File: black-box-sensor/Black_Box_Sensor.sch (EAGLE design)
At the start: 42 parts, among them J1 104031-0811, J2 UX60-MB-5S8, J3 B4B-PH-SM4-TBT(LF)(SN), U1 ADXL375, U2 ADXL375, U3 ATMEGA32U4-AU, U4 FXAS21002CQR1, U5 MIC5504-3.3YM5-TR, U6 NL27WZ32USG, U8 AD8426ACPZ-WP

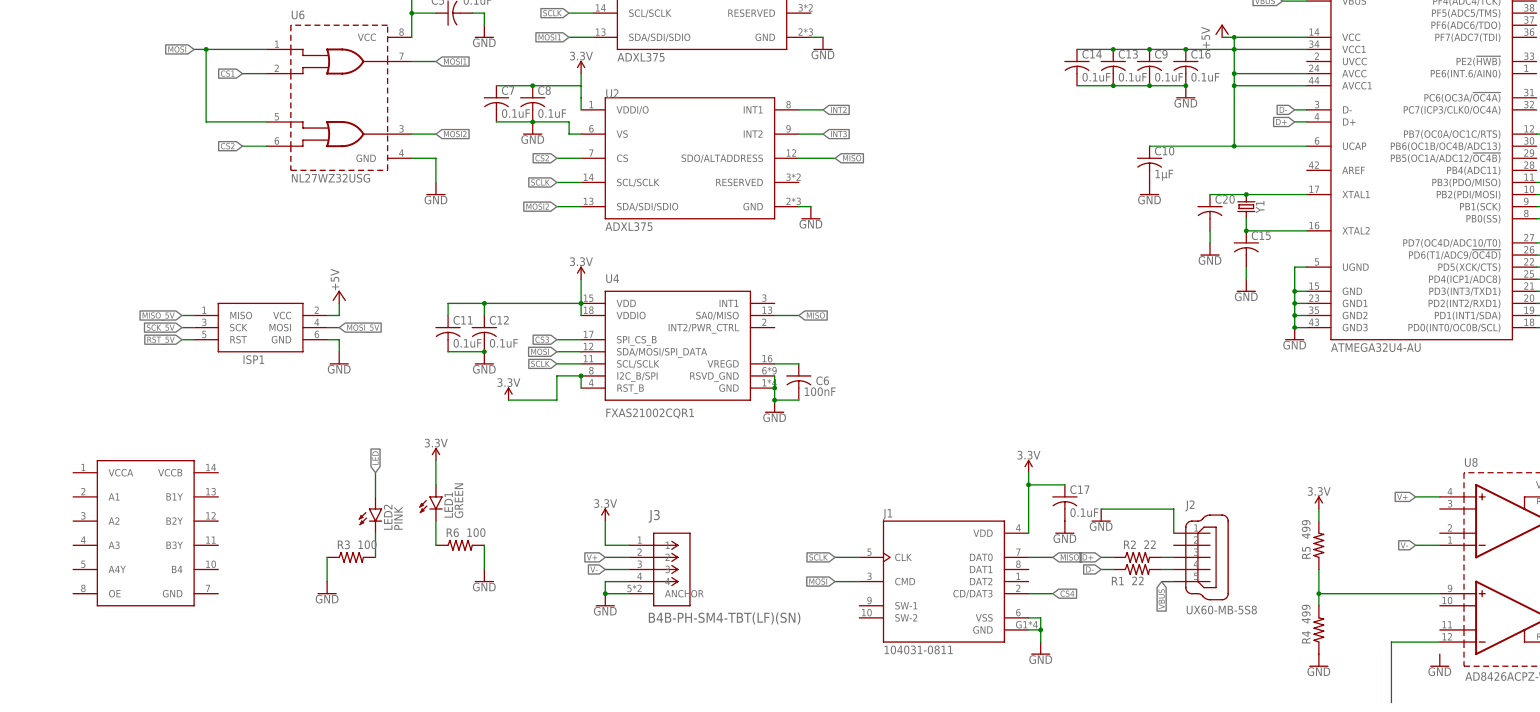
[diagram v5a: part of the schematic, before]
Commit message: label pins on level shifter
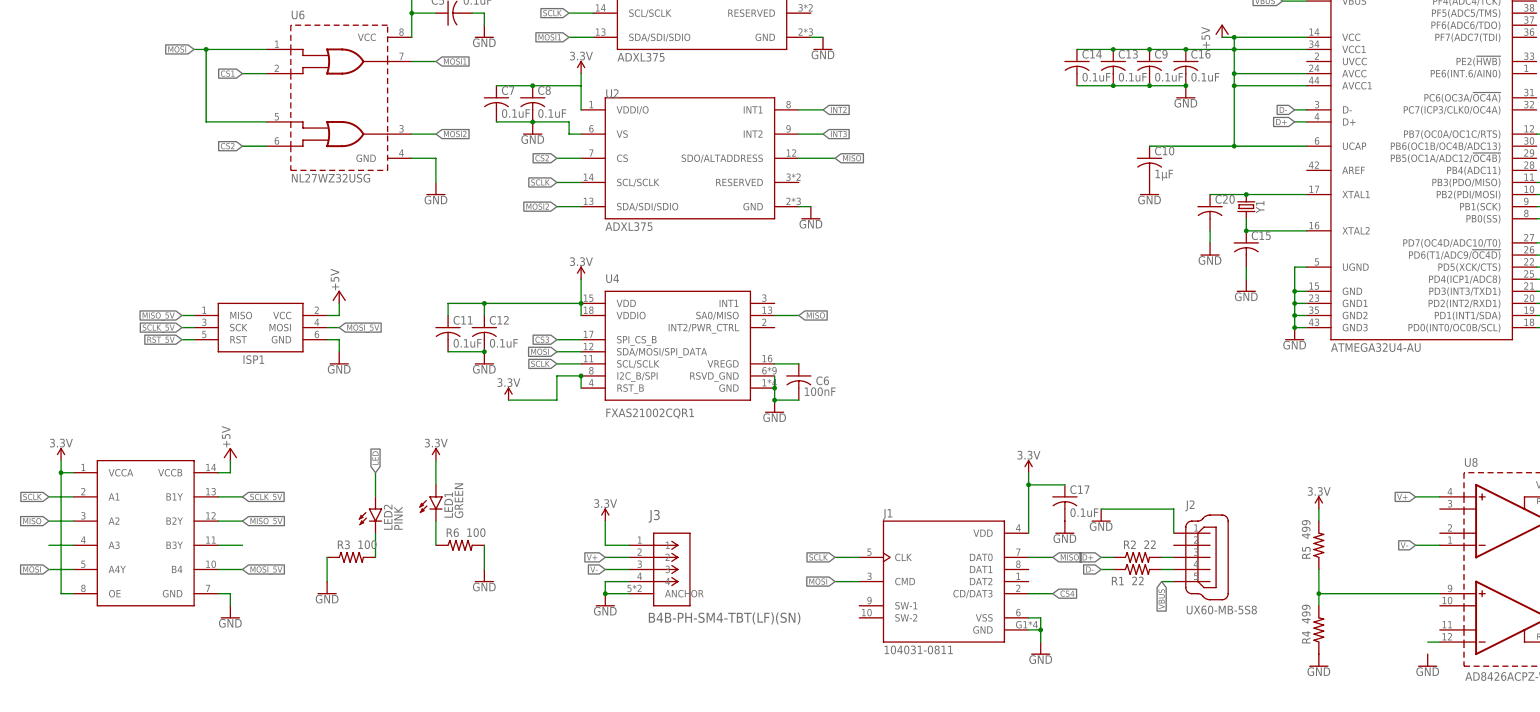
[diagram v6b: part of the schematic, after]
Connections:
- removed net SCK_5V: ISP1.SCK
- new net N$10: U$1.B3Y
- new net N$13: U$1.A3
- net +5V: now also U$1.VCCB
- net 3.3V: now also U$1.OE, U$1.VCCA
- net GND: now also U$1.GND
- net MISO: now also U$1.A2
- net MISO_5V: now also U$1.B2Y
- net MOSI: now also U$1.A4Y
- net MOSI_5V: now also U$1.B4
- net SCLK: now also U$1.A1
- net SCLK_5V: now also ISP1.SCK, U$1.B1Y
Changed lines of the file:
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@@
 <part name="GND27" library="SparkFun-PowerSymbols" deviceset="GND" device=""/>
 <part name="U$1" library="BBS_Library" deviceset="TXU0304" device=""/>
+<part name="GND28" library="SparkFun-PowerSymbols" deviceset="GND" device=""/>
+<part name="SUPPLY9" library="SparkFun-PowerSymbols" deviceset="3.3V" device=""/>
+<part name="P+4" library="supply1" library_urn="urn:adsk.eagle:library:371" deviceset="+5V" device=""/>
 </parts>
 <sheets>
@@
 <attribute name="NAME" x="-48.26" y="2.54" size="1.778" layer="95"/>
 </instance>
-<instance part="GND26" gate="1" x="203.2" y="-60.96" smashed="yes">
-<attribute name="VALUE" x="203.2" y="-61.214" size="1.778" layer="96" align="top-center"/>
+<instance part="GND26" gate="1" x="200.66" y="-60.96" smashed="yes">
+<attribute name="VALUE" x="200.66" y="-61.214" size="1.778" layer="96" align="top-center"/>
 </instance>
 <instance part="Y1" gate="G$1" x="162.56" y="35.56" smashed="yes" rot="R270">
@@
 </instance>
 <instance part="U$1" gate="G$1" x="-68.58" y="-33.02" smashed="yes"/>
+<instance part="GND28" gate="1" x="-50.8" y="-50.8" smashed="yes">
+<attribute name="VALUE" x="-50.8" y="-51.054" size="1.778" layer="96" align="top-center"/>
+</instance>
+<instance part="SUPPLY9" gate="G$1" x="-86.36" y="-17.78" smashed="yes">
+<attribute name="VALUE" x="-86.36" y="-14.986" size="1.778" layer="96" align="bottom-center"/>
+</instance>
+<instance part="P+4" gate="1" x="-50.8" y="-15.24" smashed="yes">
+<attribute name="VALUE" x="-50.8" y="-15.24" size="1.778" layer="96" rot="R90"/>
+</instance>
 </instances>
 <busses>
@@
 <pinref part="GND27" gate="1" pin="GND"/>
 </segment>
+<segment>
+<pinref part="U$1" gate="G$1" pin="GND"/>
+<wire x1="-53.34" y1="-45.72" x2="-50.8" y2="-45.72" width="0.1524" layer="91"/>
+<wire x1="-50.8" y1="-45.72" x2="-50.8" y2="-48.26" width="0.1524" layer="91"/>
+<pinref part="GND28" gate="1" pin="GND"/>
+</segment>
 </net>
 <net name="3.3V" class="0">
@@
 <segment>
 <pinref part="U2" gate="ADXL375BCCZ-RL7" pin="VDDI/O"/>
-<wire x1="22.86" y1="55.88" x2="22.86" y2="58.42" width="0.1524" layer="91"/>
 <pinref part="C8" gate="G$1" pin="1"/>
-<wire x1="22.86" y1="58.42" x2="22.86" y2="60.96" width="0.1524" layer="91"/>
+<wire x1="22.86" y1="55.88" x2="22.86" y2="60.96" width="0.1524" layer="91"/>
 <wire x1="22.86" y1="60.96" x2="12.7" y2="60.96" width="0.1524" layer="91"/>
 <pinref part="C7" gate="G$1" pin="1"/>
@@
 <pinref part="SUPPLY3" gate="G$1" pin="3.3V"/>
 </segment>
+<segment>
+<pinref part="U$1" gate="G$1" pin="VCCA"/>
+<wire x1="-83.82" y1="-20.32" x2="-86.36" y2="-20.32" width="0.1524" layer="91"/>
+<wire x1="-86.36" y1="-20.32" x2="-86.36" y2="-17.78" width="0.1524" layer="91"/>
+<pinref part="U$1" gate="G$1" pin="OE"/>
+<wire x1="-83.82" y1="-45.72" x2="-86.36" y2="-45.72" width="0.1524" layer="91"/>
+<wire x1="-86.36" y1="-45.72" x2="-86.36" y2="-20.32" width="0.1524" layer="91"/>
+<junction x="-86.36" y="-20.32"/>
+<pinref part="SUPPLY9" gate="G$1" pin="3.3V"/>
+</segment>
 </net>
 <net name="N$1" class="0">
@@
 <label x="76.2" y="-38.1" size="1.27" layer="95" rot="R180" xref="yes"/>
 </segment>
+<segment>
+<pinref part="U$1" gate="G$1" pin="A1"/>
+<wire x1="-83.82" y1="-25.4" x2="-88.9" y2="-25.4" width="0.1524" layer="91"/>
+<label x="-88.9" y="-25.4" size="1.27" layer="95" rot="R180" xref="yes"/>
+</segment>
 </net>
 <net name="MOSI1" class="0">
@@
 <wire x1="116.84" y1="-38.1" x2="121.92" y2="-38.1" width="0.1524" layer="91"/>
 <label x="121.92" y="-38.1" size="1.27" layer="95" xref="yes"/>
+</segment>
+<segment>
+<pinref part="U$1" gate="G$1" pin="A2"/>
+<wire x1="-83.82" y1="-30.48" x2="-88.9" y2="-30.48" width="0.1524" layer="91"/>
+<label x="-88.9" y="-30.48" size="1.27" layer="95" rot="R180" xref="yes"/>
 </segment>
 </net>
@@
 <label x="76.2" y="-43.18" size="1.27" layer="95" rot="R180" xref="yes"/>
 </segment>
+<segment>
+<pinref part="U$1" gate="G$1" pin="A4Y"/>
+<wire x1="-83.82" y1="-40.64" x2="-88.9" y2="-40.64" width="0.1524" layer="91"/>
+<label x="-88.9" y="-40.64" size="1.27" layer="95" rot="R180" xref="yes"/>
+</segment>
 </net>
 <net name="CS2" class="0">
@@
 <segment>
 <pinref part="U8" gate="G$1" pin="INB-"/>
-<wire x1="203.2" y1="-55.88" x2="193.04" y2="-55.88" width="0.1524" layer="91"/>
-<wire x1="193.04" y1="-55.88" x2="193.04" y2="-68.58" width="0.1524" layer="91"/>
+<wire x1="203.2" y1="-55.88" x2="200.66" y2="-55.88" width="0.1524" layer="91"/>
 </segment>
 <segment>
@@
 <wire x1="-27.94" y1="12.7" x2="-27.94" y2="15.24" width="0.1524" layer="91"/>
 </segment>
+<segment>
+<pinref part="U$1" gate="G$1" pin="VCCB"/>
+<wire x1="-53.34" y1="-20.32" x2="-50.8" y2="-20.32" width="0.1524" layer="91"/>
+<wire x1="-50.8" y1="-20.32" x2="-50.8" y2="-17.78" width="0.1524" layer="91"/>
+<pinref part="P+4" gate="1" pin="+5V"/>
+</segment>
 </net>
 <net name="MISO_5V" class="0">
@@
 <label x="226.06" y="40.64" size="1.27" layer="95" xref="yes"/>
 </segment>
-</net>
-<net name="SCK_5V" class="0">
+<segment>
+<pinref part="U$1" gate="G$1" pin="B2Y"/>
+<wire x1="-53.34" y1="-30.48" x2="-48.26" y2="-30.48" width="0.1524" layer="91"/>
+<label x="-48.26" y="-30.48" size="1.27" layer="95" xref="yes"/>
+</segment>
+</net>
+<net name="RST_5V" class="0">
+<segment>
+<pinref part="ISP1" gate="G$1" pin="RST"/>
+<wire x1="-58.42" y1="7.62" x2="-60.96" y2="7.62" width="0.1524" layer="91"/>
+<label x="-60.96" y="7.62" size="1.27" layer="95" rot="R180" xref="yes"/>
+</segment>
+</net>
+<net name="MOSI_5V" class="0">
+<segment>
+<pinref part="ISP1" gate="G$1" pin="MOSI"/>
+<wire x1="-30.48" y1="10.16" x2="-27.94" y2="10.16" width="0.1524" layer="91"/>
+<label x="-27.94" y="10.16" size="1.27" layer="95" xref="yes"/>
+</segment>
+<segment>
+<pinref part="U3" gate="G$1" pin="PB2(PDI/MOSI)"/>
+<label x="226.06" y="38.1" size="1.27" layer="95" xref="yes"/>
+<wire x1="223.52" y1="38.1" x2="226.06" y2="38.1" width="0.1524" layer="91"/>
+</segment>
+<segment>
+<pinref part="U$1" gate="G$1" pin="B4"/>
+<wire x1="-53.34" y1="-40.64" x2="-48.26" y2="-40.64" width="0.1524" layer="91"/>
+<label x="-48.26" y="-40.64" size="1.27" layer="95" xref="yes"/>
+</segment>
+</net>
+<net name="SCLK_5V" class="0">
+<segment>
+<pinref part="U3" gate="G$1" pin="PB1(SCK)"/>
+<wire x1="223.52" y1="35.56" x2="226.06" y2="35.56" width="0.1524" layer="91"/>
+<label x="226.06" y="35.56" size="1.27" layer="95" xref="yes"/>
+</segment>
 <segment>
 <pinref part="ISP1" gate="G$1" pin="SCK"/>
@@
 <label x="-60.96" y="10.16" size="1.27" layer="95" rot="R180" xref="yes"/>
 </segment>
-</net>
-<net name="RST_5V" class="0">
-<segment>
-<pinref part="ISP1" gate="G$1" pin="RST"/>
-<wire x1="-58.42" y1="7.62" x2="-60.96" y2="7.62" width="0.1524" layer="91"/>
-<label x="-60.96" y="7.62" size="1.27" layer="95" rot="R180" xref="yes"/>
-</segment>
-</net>
-<net name="MOSI_5V" class="0">
-<segment>
-<pinref part="ISP1" gate="G$1" pin="MOSI"/>
-<wire x1="-30.48" y1="10.16" x2="-27.94" y2="10.16" width="0.1524" layer="91"/>
-<label x="-27.94" y="10.16" size="1.27" layer="95" xref="yes"/>
-</segment>
-<segment>
-<pinref part="U3" gate="G$1" pin="PB2(PDI/MOSI)"/>
-<label x="226.06" y="38.1" size="1.27" layer="95" xref="yes"/>
-<wire x1="223.52" y1="38.1" x2="226.06" y2="38.1" width="0.1524" layer="91"/>
-</segment>
-</net>
-<net name="SCLK_5V" class="0">
-<segment>
-<pinref part="U3" gate="G$1" pin="PB1(SCK)"/>
-<wire x1="223.52" y1="35.56" x2="226.06" y2="35.56" width="0.1524" layer="91"/>
-<label x="226.06" y="35.56" size="1.27" layer="95" xref="yes"/>
-</segment>
-</net>
+<segment>
+<pinref part="U$1" gate="G$1" pin="B1Y"/>
+<wire x1="-53.34" y1="-25.4" x2="-48.26" y2="-25.4" width="0.1524" layer="91"/>
+<label x="-48.26" y="-25.4" size="1.27" layer="95" xref="yes"/>
+</segment>
+</net>
+<net name="N$10" class="0">
+<segment>
+<pinref part="U$1" gate="G$1" pin="B3Y"/>
+<wire x1="-53.34" y1="-35.56" x2="-48.26" y2="-35.56" width="0.1524" layer="91"/>
+</segment>
+</net>
+<net name="N$13" class="0">
+<segment>
+<pinref part="U$1" gate="G$1" pin="A3"/>
+<wire x1="-83.82" y1="-35.56" x2="-88.9" y2="-35.56" width="0.1524" layer="91"/>
+</segment>
+</net>

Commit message: add receiver connector and level shifting
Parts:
- added JP1: (no value), pinhead:PINHD-1X3
- added R10, R11, R7, R8, R9: 19.3k, rcl:R-US_R0603
- added R12, R13, R14, R15: 10k, rcl:R-US_R0603
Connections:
- removed net N$10: U$1.B3Y
- removed net N$13: U$1.A3
- new net CS1_5V: R12.2, U3.PB0(SS)
- new net CS2_5V: R13.2, U3.PB7(OC0A/OC1C/RTS)
- new net CS3_5V: R14.2, U3.PD4(ICP1/ADC8)
- new net CS4_5V: R15.2, U3.PD5(XCK/CTS)
- new net N$8: R7.1, U8.REFB
- new net OE: U$1.OE
- new net RECEIVER: JP1.2, U3.PF0(ADC0)
- net +5V: now also C1.1, JP1.1, U5.EN, U5.VIN
- net 3.3V: no longer U$1.OE
- net CS1: now also R10.2, R12.1; no longer U3.PB0(SS)
- net CS2: now also R11.2, R13.1; no longer U3.PB7(OC0A/OC1C/RTS)
- net CS3: now also R14.1, R8.2; no longer U3.PD4(ICP1/ADC8)
- net CS4: now also R15.1, R9.2; no longer U3.PD5(XCK/CTS)
- net GND: now also JP1.3, R10.1, R11.1, R7.2, R8.1, R9.1, U8.INB-
- net VBATT: no longer C1.1, U5.EN, U5.VIN
- net VREF/2: no longer U8.INB-
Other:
- moved on the sheet: C1, C17, C2, J1, J2, R1, R2
